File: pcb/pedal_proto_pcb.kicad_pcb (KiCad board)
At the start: 2 copper layers, 90 x 70 mm, 36 parts, among them J1 100k_pot_1, J10 100k_pot_1_B, J11 100k_pot_1_C, J12 100k_pot_2_A, J13 100k_pot_2_B, J14 100k_pot_2_C, J15 250k_pot_1_A, J16 250k_pot_1_B, J17 250k_pot_1_C, J18 250k_pot_2_A, J19 250k_pot_2_B, J2 100k_pot_2, J20 250k_pot_2_C, J21 stomp_1_A, J22 stomp_1_B, J23 stomp_1_C, J24 stomp_2_A, J25 stomp_2_B, J26 stomp_2_C, J27 stomp_3_A, J28 stomp_3_B, J29 stomp_2_C, J3 250k_pot_1, J30 switch_A, J31 switch_B, J32 switch_C, J33 GND, J34 VDD, J35 LED-, J36 LED+, J4 250k_pot_2, J5 stomp, J6 switch, J7 power, J8 LED, J9 100k_pot_1_A

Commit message: feat: updated pcb
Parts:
- removed J1: 100k_pot_1, Connector_PinHeader_2.54mm:PinHeader_1x04_P2.54mm_Vertical
- removed J2: 100k_pot_2, Connector_PinHeader_2.54mm:PinHeader_1x04_P2.54mm_Vertical
- removed J3: 250k_pot_1, Connector_PinHeader_2.54mm:PinHeader_1x04_P2.54mm_Vertical
- removed J4: 250k_pot_2, Connector_PinHeader_2.54mm:PinHeader_1x04_P2.54mm_Vertical
- removed J8: LED, Connector_PinHeader_2.54mm:PinHeader_1x02_P2.54mm_Vertical
- added D1: LED, LED_THT:LED_D4.0mm, F.Cu at (199.5, 131.0)
- added J38: input, Connector_PinHeader_2.54mm:PinHeader_1x02_P2.54mm_Vertical, F.Cu at (123.5, 144.7)
- added J39: output, Connector_PinHeader_2.54mm:PinHeader_1x02_P2.54mm_Vertical, F.Cu at (216.0, 145.0)
- added RV1: 100k_Potentiometer, Additional_Switches:Lug_Pot, F.Cu at (132.0, 51.6)
- added RV2: 100k_Potentiometer, Additional_Switches:Lug_Pot, F.Cu at (157.0, 51.1)
- added RV3: 250k_Potentiometer, Additional_Switches:Lug_Pot, F.Cu at (182.0, 51.6)
- added RV4: 250k_Potentiometer, Additional_Switches:Lug_Pot, F.Cu at (207.0, 51.6)
- added SW1: SW_3PDT, Additional_Switches:3PDT, F.Cu at (144.5, 89.5)
- added SW2: SW_SPDT, Additional_Switches:SPDT, F.Cu at (179.5, 104.5)
- J10: value 100k_pot_1_B -> RV1_2
- J11: value 100k_pot_1_C -> RV1_1
- J12: value 100k_pot_2_A -> RV2_3
- J13: value 100k_pot_2_B -> RV2_2
- J14: value 100k_pot_2_C -> RV2_1
- J15: value 250k_pot_1_A -> RV3_3
- J16: value 250k_pot_1_B -> RV3_2
- J17: value 250k_pot_1_C -> RV3_1
- J18: value 250k_pot_2_A -> RV4_3
- J19: value 250k_pot_2_B -> RV4_2
- J20: value 250k_pot_2_C -> RV4_1
- J21: value stomp_1_A -> stomp_A_1
- J22: value stomp_1_B -> stomp_A_2
- J23: value stomp_1_C -> stomp_A_3
- J24: value stomp_2_A -> stomp_B_1
- J25: value stomp_2_B -> stomp_B_2
- J26: value stomp_2_C -> stomp_B_3
- J27: value stomp_3_A -> stomp_C_1
- J28: value stomp_3_B -> stomp_C_2
- J29: value stomp_2_C -> stomp_C_3
- J30: value switch_A -> switch_1
- J31: value switch_B -> switch_2
- J32: value switch_C -> switch_3
- J5: value stomp -> Jack-DC; footprint Connector_PinHeader_2.54mm:PinHeader_1x10_P2.54mm_Vertical -> Additional_Connectors:Barrel_Plug_5.5mmx2.1mm
- J6: value switch -> Barrel_Jack_Output; footprint Connector_PinHeader_2.54mm:PinHeader_1x04_P2.54mm_Vertical -> Connector_PinHeader_2.54mm:PinHeader_1x02_P2.54mm_Vertical
- J7: value power -> Barrel_Jack_Input
- J9: value 100k_pot_1_A -> RV1_3
- moved J7 87.8 mm to (122.5, 103.2), turned to 0 degrees
- moved J6 48.1 mm to (216.5, 103.2), turned to 0 degrees
- moved J5 45.2 mm to (195.5, 94.5), turned to 0 degrees
- moved J35 29.0 mm to (201.0, 145.2)
- moved J36 29.0 mm to (196.0, 145.2)
- moved J10 28.7 mm to (137.5, 136.7)
- moved J11 28.7 mm to (137.5, 145.0)
- moved J13 28.7 mm to (142.5, 136.7)
- moved J14 28.7 mm to (142.5, 145.0)
- moved J16 28.7 mm to (147.5, 136.7)
- moved J17 28.7 mm to (147.5, 145.0)
- moved J19 28.7 mm to (152.5, 136.7)
- moved J20 28.7 mm to (152.5, 145.0)
- moved J21 28.7 mm to (165.0, 145.0)
- moved J22 28.7 mm to (165.0, 136.7)
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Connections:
- J34 pad 1: /VDD -> Net-(J34-Pin_1)
- J34 pad 2: /VDD -> Net-(J34-Pin_1)
- J5 pad 1: 0 -> Net-(J34-Pin_1)
- J5 pad 2: Net-(J21-Pin_1) -> 0
- J6 pad 2: Net-(J30-Pin_1) -> Net-(J39-Pin_1)
- J7 pad 2: /VDD -> Net-(J38-Pin_1)
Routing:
- net Net-(J27-Pin_1): track 67.2 -> 2.54 mm
- net Net-(J24-Pin_1): track 66.1 -> 2.54 mm
- net Net-(J21-Pin_1): track 64.8 -> 2.54 mm
- net Net-(J20-Pin_1): track 63.8 -> 2.54 mm
- net Net-(J14-Pin_1): track 61.2 -> 2.54 mm
- net /VDD: track 58.6 -> 0.00 mm
- net Net-(J28-Pin_1): track 58.9 -> 2.54 mm
- net Net-(J25-Pin_1): track 57.8 -> 2.54 mm
- net Net-(J22-Pin_1): track 57.2 -> 2.54 mm
- net Net-(J19-Pin_1): track 56.1 -> 2.54 mm
- net Net-(D1-A): track 50.6 -> 0.00 mm
- net Net-(J13-Pin_1): track 53.2 -> 2.54 mm
- net Net-(J17-Pin_1): track 53.1 -> 2.54 mm
- net Net-(J30-Pin_1): track 52.7 -> 2.54 mm
- net Net-(D1-K): track 49.6 -> 0.00 mm
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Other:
- board size 90 x 70 mm -> 100 x 100 mm

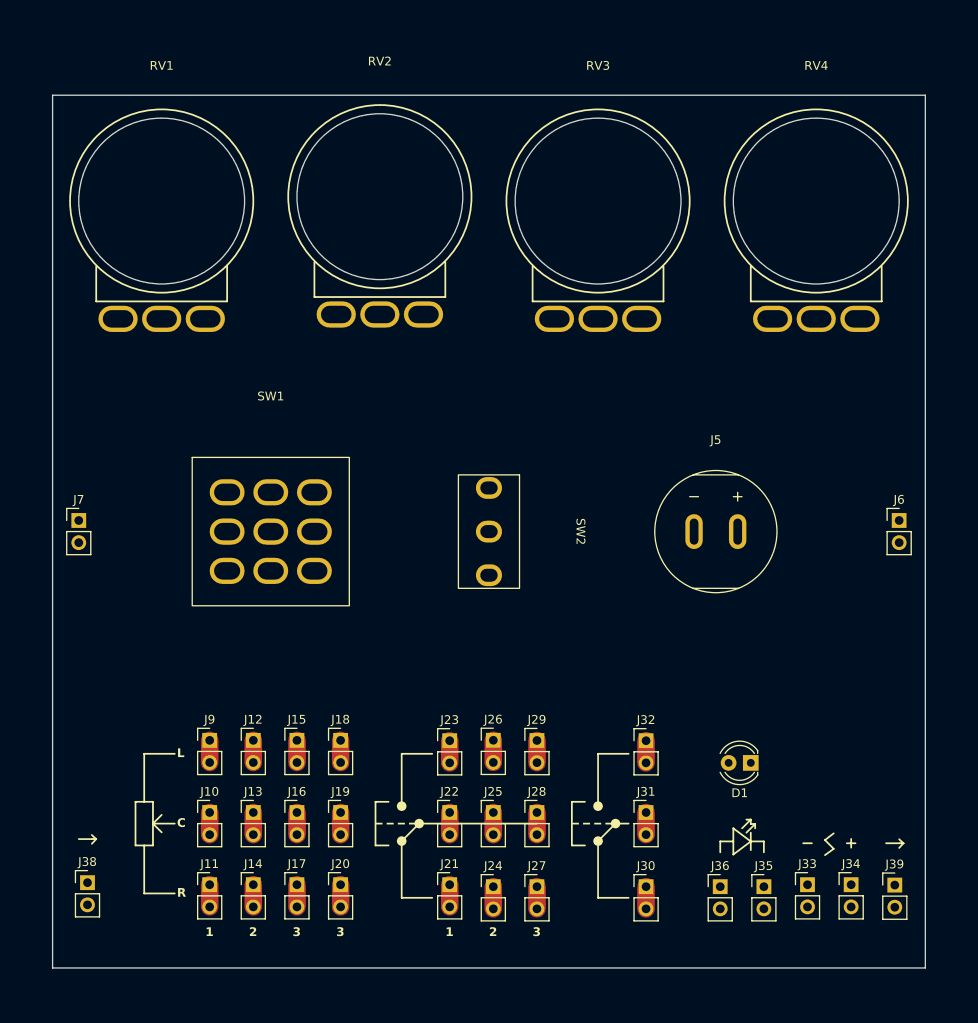
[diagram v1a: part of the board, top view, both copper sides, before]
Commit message: feat: added GND, pwr led and prw switch
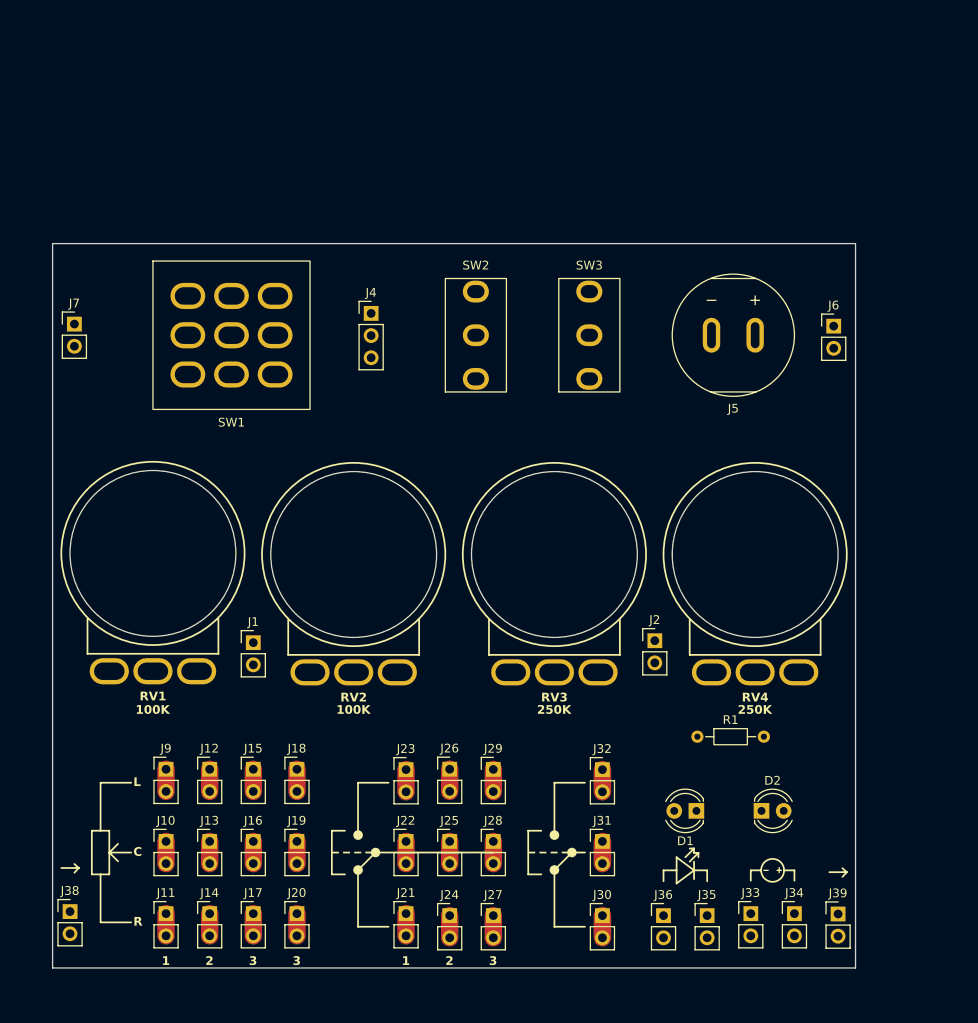
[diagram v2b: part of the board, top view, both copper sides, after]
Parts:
- added D2: LED, LED_THT:LED_D4.0mm, F.Cu at (200.7, 136.5)
- added J1: GND, Connector_PinHeader_2.54mm:PinHeader_1x02_P2.54mm_Vertical, F.Cu at (142.5, 117.2)
- added J2: GND, Connector_PinHeader_2.54mm:PinHeader_1x02_P2.54mm_Vertical, F.Cu at (188.5, 117.0)
- added J4: Conn_01x03_Socket, Connector_PinHeader_2.54mm:PinHeader_1x03_P2.54mm_Vertical, F.Cu at (156.0, 79.5)
- added R1: R, Resistor_THT:R_Axial_DIN0204_L3.6mm_D1.6mm_P7.62mm_Horizontal, F.Cu at (193.4, 128.0)
- added SW3: SW_SPDT, Additional_Switches:SPDT, F.Cu at (171.0, 82.0)
- moved RV2 41.1 mm to (154.0, 92.1)
- moved RV4 41.1 mm to (200.0, 92.1)
- moved RV3 40.8 mm to (177.0, 92.1)
- moved RV1 40.4 mm to (131.0, 92.0)
- moved SW2 31.1 mm to (158.0, 82.0), turned to 90 degrees
- moved J6 23.5 mm to (209.0, 81.0)
- moved SW1 22.9 mm to (140.0, 67.0)
- moved J5 22.6 mm to (197.5, 72.0)
- moved J7 22.5 mm to (122.0, 80.7)
- moved D1 8.31 mm to (193.3, 136.5)
- moved J33 7.30 mm to (199.5, 148.3)
- moved J34 7.30 mm to (204.5, 148.3)
- moved J35 7.30 mm to (194.5, 148.5)
- moved J36 7.30 mm to (189.5, 148.5)
- moved J39 7.30 mm to (209.5, 148.3)
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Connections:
- J5 pad 1: Net-(J34-Pin_1) -> Net-(SW3-B)
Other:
- board size 100 x 100 mm -> 92 x 83 mm
- board text added: "100K"
- board text added: "250K"

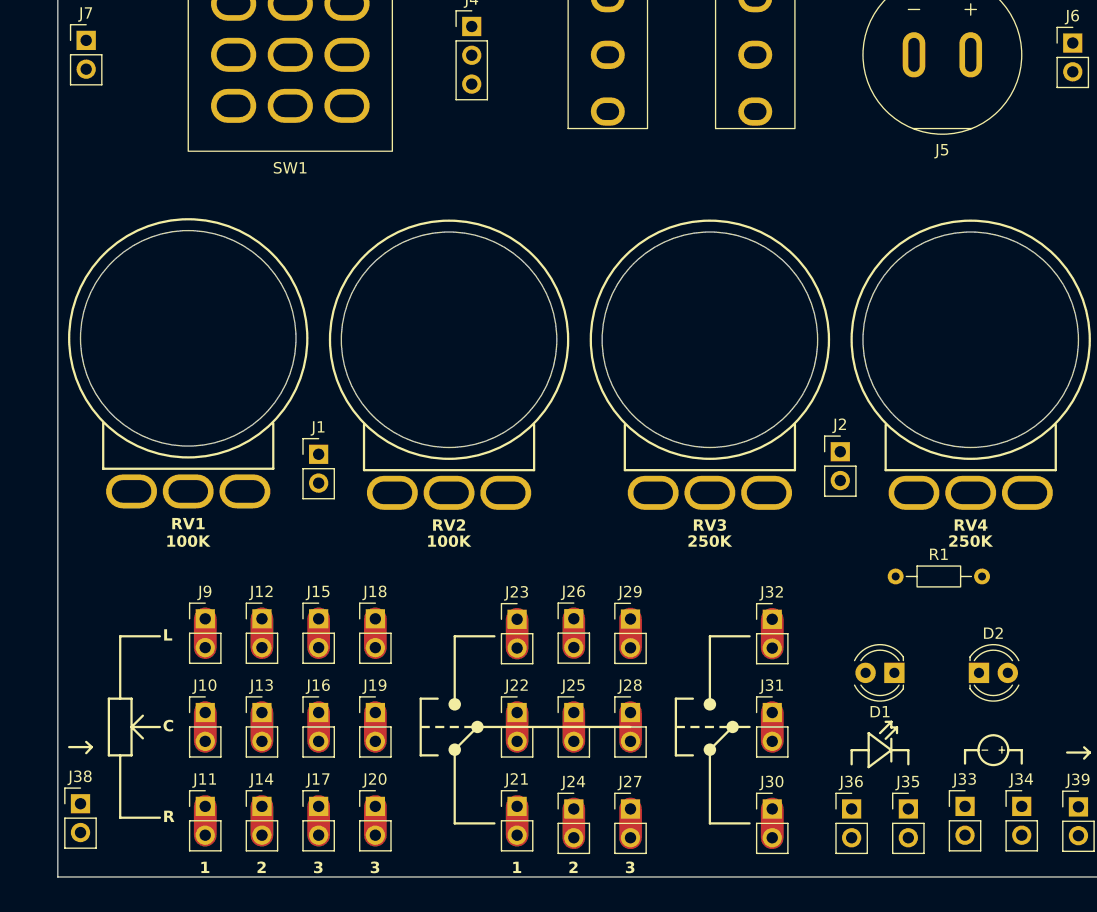
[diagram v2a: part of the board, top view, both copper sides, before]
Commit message: feat: began routing
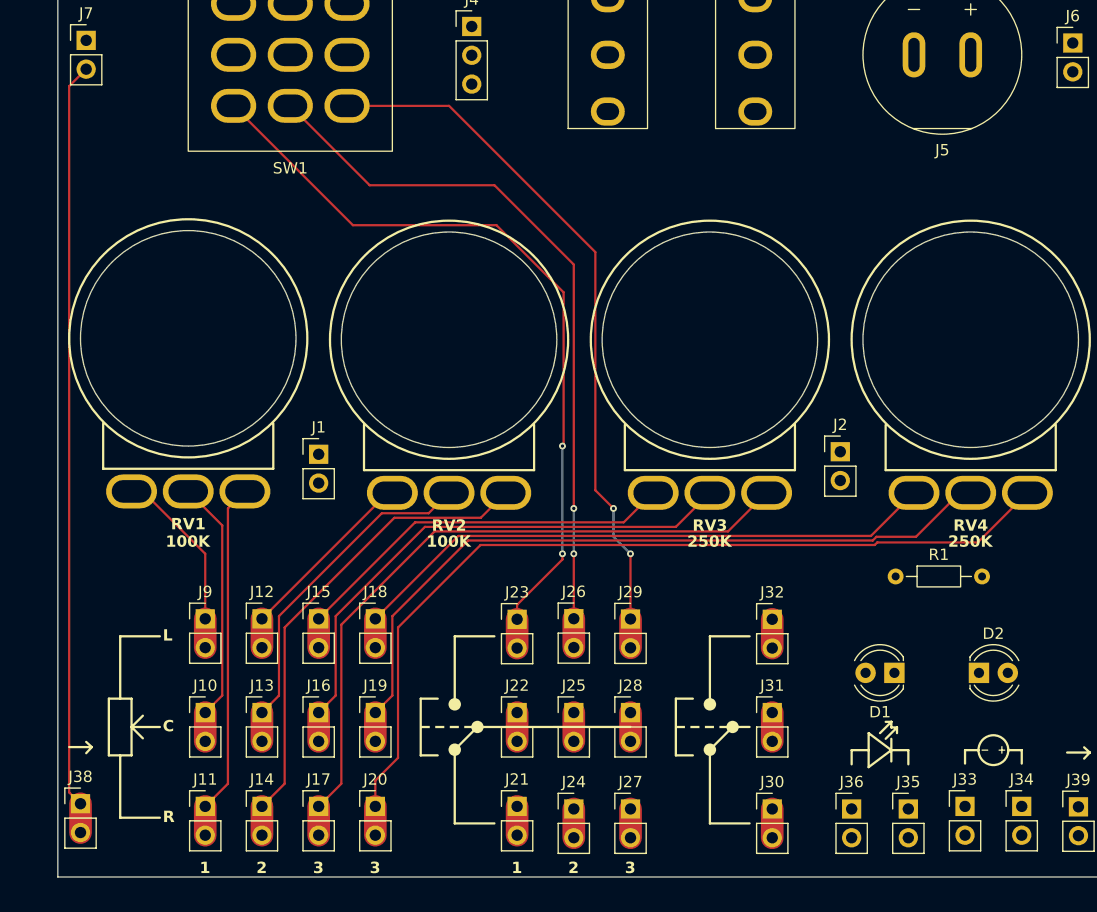
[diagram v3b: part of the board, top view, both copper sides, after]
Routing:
- net Net-(J20-Pin_1): track 2.54 -> 79.6 mm
- net Net-(J38-Pin_1): track 0.00 -> 68.4 mm
- net Net-(J23-Pin_1): track 2.54 -> 69.0 mm, vias 0 -> 2
- net Net-(J19-Pin_1): track 2.54 -> 67.2 mm
- net Net-(J26-Pin_1): track 2.54 -> 64.6 mm, vias 0 -> 2
- net Net-(J29-Pin_1): track 2.54 -> 63.4 mm, vias 0 -> 2
- net Net-(J17-Pin_1): track 2.54 -> 61.7 mm
- net Net-(J18-Pin_1): track 2.54 -> 54.6 mm
- net Net-(J16-Pin_1): track 2.54 -> 49.2 mm
- net Net-(J14-Pin_1): track 2.54 -> 43.6 mm
- net Net-(J15-Pin_1): track 2.54 -> 36.6 mm
- net Net-(J11-Pin_1): track 2.54 -> 31.8 mm
- net Net-(J13-Pin_1): track 2.54 -> 31.2 mm
- net Net-(J10-Pin_1): track 2.54 -> 23.9 mm
- net Net-(J9-Pin_1): track 2.54 -> 19.6 mm
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
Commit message: feat: almost done
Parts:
- added J3: GND, Connector_PinHeader_2.54mm:PinHeader_1x01_P2.54mm_Vertical, F.Cu at (170.5, 93.0)
- added J37: GND, Connector_PinHeader_2.54mm:PinHeader_1x01_P2.54mm_Vertical, F.Cu at (154.0, 82.0)
- added J40: GND, Connector_PinHeader_2.54mm:PinHeader_1x01_P2.54mm_Vertical, F.Cu at (174.5, 82.0)
- added J8: GND, Connector_PinHeader_2.54mm:PinHeader_1x01_P2.54mm_Vertical, F.Cu at (158.5, 82.0)
- added R2: 330, Resistor_THT:R_Axial_DIN0309_L9.0mm_D3.2mm_P12.70mm_Horizontal, F.Cu at (190.3, 130.0)
- J1, J2: footprint Connector_PinHeader_2.54mm:PinHeader_1x02_P2.54mm_Vertical -> Connector_PinHeader_2.54mm:PinHeader_1x01_P2.54mm_Vertical
- J4: value Conn_01x03_Socket -> GND; footprint Connector_PinHeader_2.54mm:PinHeader_1x03_P2.54mm_Vertical -> Connector_PinHeader_2.54mm:PinHeader_1x01_P2.54mm_Vertical
- R1: value R -> 330; footprint Resistor_THT:R_Axial_DIN0204_L3.6mm_D1.6mm_P7.62mm_Horizontal -> Resistor_THT:R_Axial_DIN0309_L9.0mm_D3.2mm_P12.70mm_Horizontal
- moved D2 50.9 mm to (210.0, 86.5), turned to 180 degrees
- moved J2 47.5 mm to (147.5, 93.0)
- moved J4 40.8 mm to (194.5, 93.0)
- moved R1 39.2 mm to (211.0, 93.0), turned to 180 degrees
- moved J1 30.5 mm to (124.0, 93.0)
- moved D1 4.73 mm to (198.0, 136.5)
- moved J6 4.49 mm to (211.5, 77.2)
- moved J7 3.54 mm to (122.5, 77.2)
- moved RV4 2.00 mm to (202.0, 92.2)
- moved J39 2.00 mm to (211.5, 148.3)
- moved RV2 1.51 mm to (155.5, 92.0)
- moved RV3 1.51 mm to (178.5, 92.2)
- moved J38 1.02 mm to (122.5, 148.2)
- moved RV1 1.00 mm to (132.0, 92.0)
- moved SW2 1.00 mm to (157.0, 82.0)
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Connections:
- J36 pad 1: Net-(D1-A) -> Net-(J36-Pin_1)
- J36 pad 2: Net-(D1-A) -> Net-(J36-Pin_1)
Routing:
- net Net-(J34-Pin_1): track 0.00 -> 102.1 mm, vias 0 -> 2
- net Net-(J24-Pin_1): track 2.54 -> 101.6 mm, vias 0 -> 6
- net Net-(J21-Pin_1): track 2.54 -> 86.6 mm, vias 0 -> 2
- net Net-(J27-Pin_1): track 2.54 -> 86.5 mm, vias 0 -> 2
- net Net-(J25-Pin_1): track 2.54 -> 85.0 mm, vias 0 -> 4
- net Net-(J32-Pin_1): track 2.54 -> 79.3 mm, vias 0 -> 2
- net Net-(J28-Pin_1): track 2.54 -> 75.9 mm, vias 0 -> 2
- net Net-(J39-Pin_1): track 0.00 -> 72.7 mm
- net Net-(J22-Pin_1): track 2.54 -> 73.9 mm, vias 0 -> 2
- net Net-(J30-Pin_1): track 2.54 -> 71.4 mm, vias 0 -> 2
- net Net-(J31-Pin_1): track 2.54 -> 69.7 mm, vias 0 -> 2
- net Net-(J36-Pin_1): track 0.00 -> 21.0 mm
- net Net-(D1-K): track 0.00 -> 15.7 mm
- net Net-(D1-A): track 0.00 -> 13.1 mm
- net Net-(SW3-B): track 0.00 -> 13.0 mm
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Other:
- board size 92 x 83 mm -> 100 x 85 mm
- board text added: "FT1"
- board text added: "FT2"
- board text added: "FT3"
- board text added: "GND"
- board text added: "IN"
- board text added: "LED"
- board text added: "LED+"
- board text added: "LED-"
- board text added: "ON"
- board text added: "OUT"
- board text added: "POT1"
- board text added: "POT2"
- board text added: "POT3"
- board text added: "POT4"
- board text added: "SWITCH"
- board text added: "VDD"
- board text removed: "1"
- board text removed: "2"
- board text removed: "3"

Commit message: feat: layout done
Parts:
- moved SW2 18.0 mm to (175.0, 82.0), turned to -90 degrees
- moved R1 13.2 mm to (197.8, 92.5)
- moved J4 6.73 mm to (199.0, 98.0)
- moved J3 6.10 mm to (174.0, 98.0)
- moved J5 6.00 mm to (191.5, 72.0)
- moved J6 5.70 mm to (216.0, 80.7)
- moved D2 5.68 mm to (206.5, 82.0)
- moved J2 5.22 mm to (149.0, 98.0)
- moved RV4 5.15 mm to (207.0, 93.5)
- moved J1 5.00 mm to (124.0, 98.0)
- moved J39 4.50 mm to (216.0, 148.3)
- moved SW3 4.50 mm to (167.5, 82.0)
- moved D1 4.00 mm to (202.0, 136.5)
- moved J33 4.00 mm to (203.5, 148.2)
- moved J34 4.00 mm to (208.5, 148.2)
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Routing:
- net Net-(J34-Pin_1): track 102.1 -> 2.54 mm, vias 2 -> 0
- net Net-(J24-Pin_1): track 101.6 -> 2.54 mm, vias 6 -> 0
- net Net-(J21-Pin_1): track 86.6 -> 2.54 mm, vias 2 -> 0
- net Net-(J27-Pin_1): track 86.5 -> 2.54 mm, vias 2 -> 0
- net Net-(J25-Pin_1): track 85.0 -> 2.54 mm, vias 4 -> 0
- net Net-(J20-Pin_1): track 83.1 -> 2.54 mm
- net Net-(J32-Pin_1): track 79.3 -> 2.54 mm, vias 2 -> 0
- net Net-(J28-Pin_1): track 75.9 -> 2.54 mm, vias 2 -> 0
- net Net-(J39-Pin_1): track 72.7 -> 0.00 mm
- net Net-(J38-Pin_1): track 72.2 -> 0.00 mm
- net Net-(J22-Pin_1): track 73.9 -> 3.04 mm, vias 2 -> 0
- net Net-(J30-Pin_1): track 71.4 -> 2.54 mm, vias 2 -> 0
- net Net-(J19-Pin_1): track 71.2 -> 2.54 mm
- net Net-(J31-Pin_1): track 69.7 -> 2.54 mm, vias 2 -> 0
- net Net-(J17-Pin_1): track 63.9 -> 2.54 mm
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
